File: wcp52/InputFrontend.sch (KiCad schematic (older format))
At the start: 8 parts

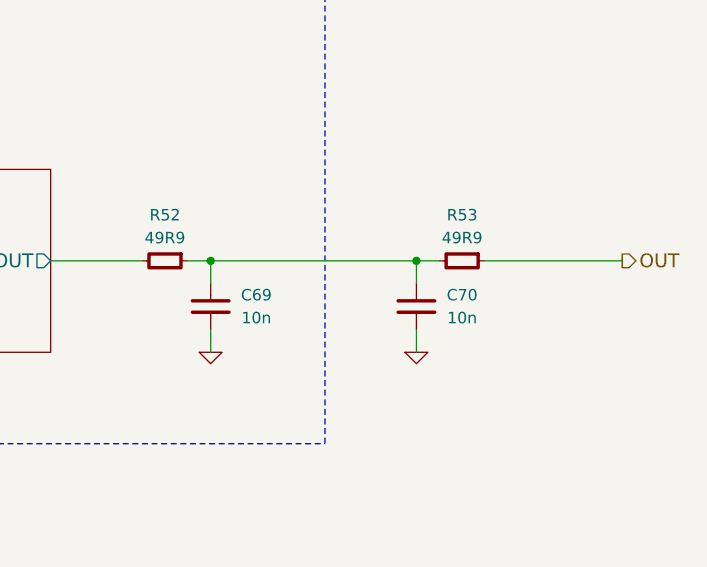
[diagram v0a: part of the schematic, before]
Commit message: Add PSU filter inductors
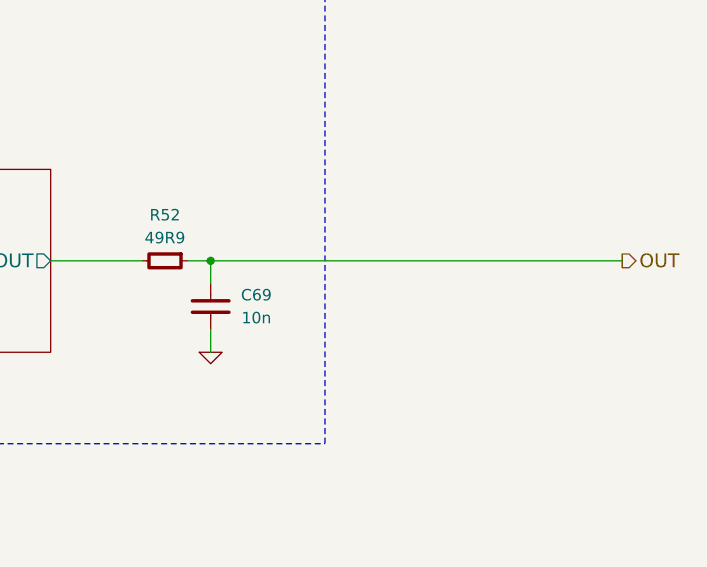
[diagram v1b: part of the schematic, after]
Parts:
- removed C70: 10n, IPC7351-Nominal:CAPC1608X55, symbol C-0603
- removed R53: 49R9, IPC7351-Nominal:RESC1608X50, symbol R-0603
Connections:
- net OUT: now also C69.1, R52.1
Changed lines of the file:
@@
 $EndComp
 $Comp
-L GND #PWR0150
+L GND #PWR0151
 U 1 1 54F2F4A0
 P 3500 4300
-F 0 "#PWR0150" H 3500 4300 30  0001 C CNN
+F 0 "#PWR0151" H 3500 4300 30  0001 C CNN
 F 1 "GND" H 3500 4230 30  0001 C CNN
 F 2 "" H 3500 4300 60  0000 C CNN
@@
 	10300 1200 3200 1200
 Wire Wire Line
-	9700 3400 10800 3400
+	9700 3400 11600 3400
 Wire Wire Line
 	9800 3400 9800 3500
 Connection ~ 9800 3400
-Wire Wire Line
-	10700 3400 10700 3500
-Connection ~ 10700 3400
 Text HLabel 11600 3400 2    60   Output ~ 0
 OUT
-Wire Wire Line
-	11600 3400 11000 3400
-$Comp
-L GND #PWR0151
+$Comp
+L GND #PWR0152
 U 1 1 54F3075A
 P 9800 3800
-F 0 "#PWR0151" H 9800 3800 30  0001 C CNN
+F 0 "#PWR0152" H 9800 3800 30  0001 C CNN
 F 1 "GND" H 9800 3730 30  0001 C CNN
 F 2 "" H 9800 3800 60  0000 C CNN
@@
 Wire Wire Line
 	9800 3700 9800 3800
-$Comp
-L GND #PWR0152
-U 1 1 54F3079D
-P 10700 3800
-F 0 "#PWR0152" H 10700 3800 30  0001 C CNN
-F 1 "GND" H 10700 3730 30  0001 C CNN
-F 2 "" H 10700 3800 60  0000 C CNN
-F 3 "" H 10700 3800 60  0000 C CNN
-	1    10700 3800
-	1    0    0    -1
-$EndComp
-Wire Wire Line
-	10700 3800 10700 3700
 Wire Wire Line
 	4300 3200 1800 3200
@@
 F 5 "CAP MLCC 10n ≥X5R 50V 10% [0603]" H 10600 4150 60  0001 C CNN "BOM"
 	1    9800 3600
-	1    0    0    -1
-$EndComp
-$Comp
-L C-0603 C70
-U 1 1 55033D91
-P 10700 3600
-F 0 "C70" H 10900 3650 50  0000 C CNN
-F 1 "10n" H 10900 3550 50  0000 C CNN
-F 2 "IPC7351-Nominal:CAPC1608X55" H 10700 3600 50  0001 C CNN
-F 3 "" H 10690 3575 60  0000 C CNN
-F 4 "Value" H 10700 3600 60  0001 C CNN "Manuf"
-F 5 "CAP MLCC 10n ≥X5R 50V 10% [0603]" H 11500 4150 60  0001 C CNN "BOM"
-	1    10700 3600
 	1    0    0    -1
 $EndComp
@@
 	0    1    1    0
 $EndComp
-$Comp
-L R-0603 R53
-U 1 1 550340A6
-P 10900 3400
-F 0 "R53" V 10700 3400 50  0000 C CNN
-F 1 "49R9" V 10800 3400 50  0000 C CNN
-F 2 "IPC7351-Nominal:RESC1608X50" H 10900 3400 50  0001 C CNN
-F 3 "" H 10900 3450 60  0000 C CNN
-F 4 "Value" H 10900 3400 60  0001 C CNN "Manuf"
-F 5 "RES SMD 49R9 1% [0603]" H 11650 3950 60  0001 C CNN "BOM"
-	1    10900 3400
-	0    1    1    0
-$EndComp

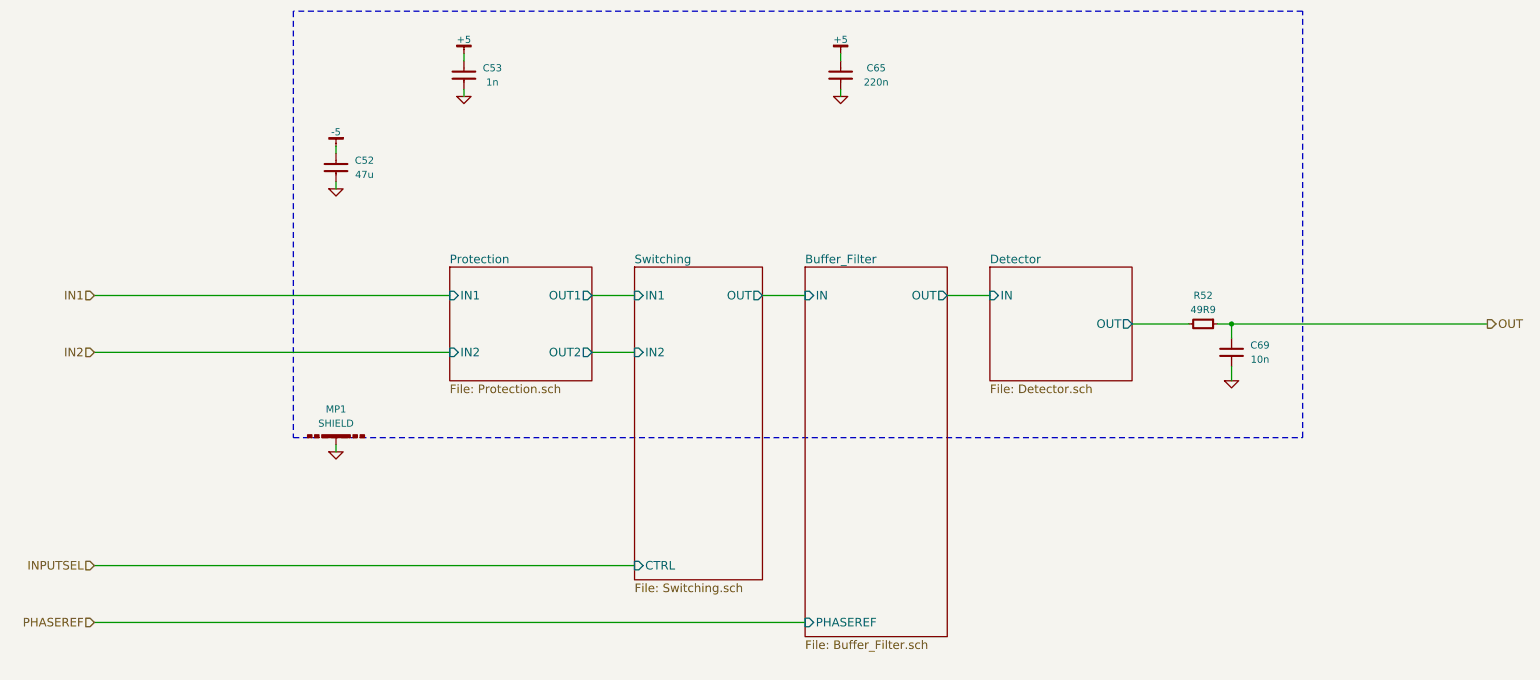
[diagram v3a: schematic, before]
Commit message: Reannotate parts. May need to tweak silkscreen
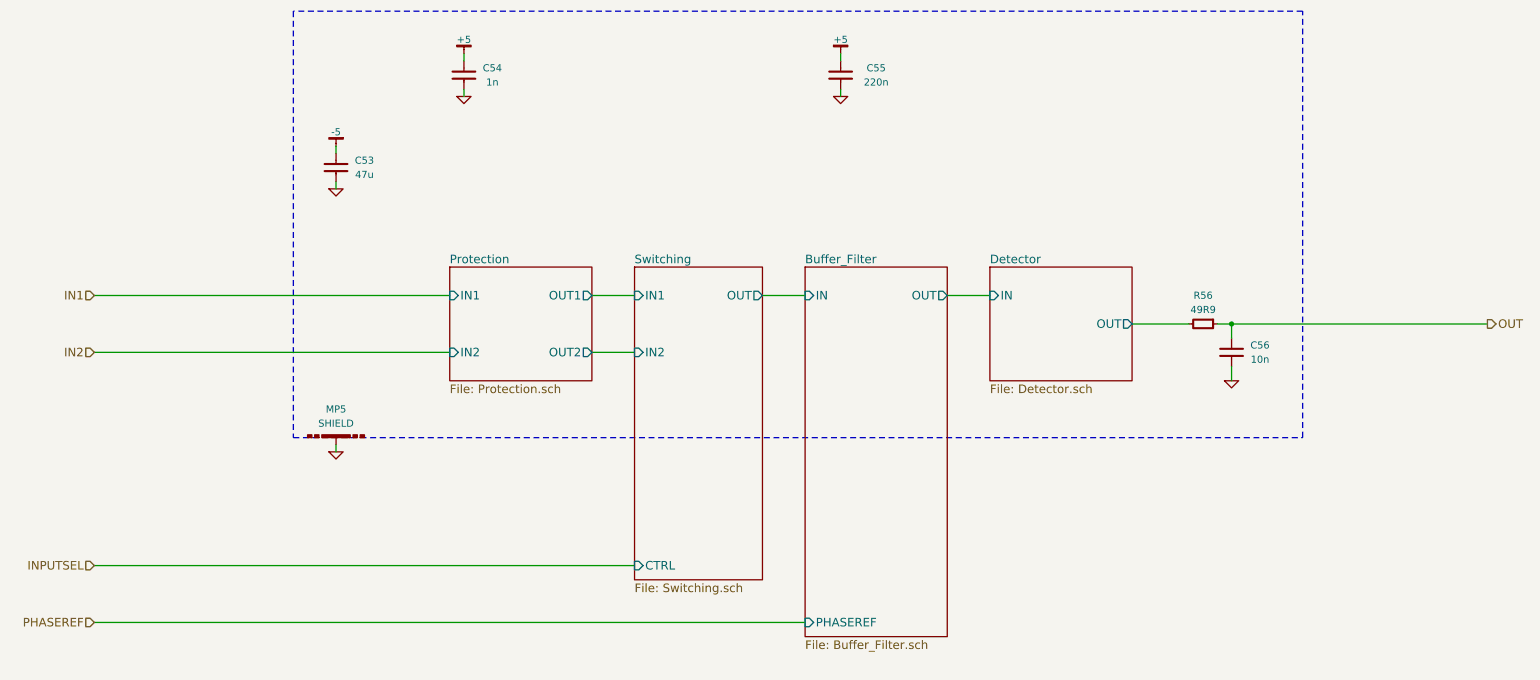
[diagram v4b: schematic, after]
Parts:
- C53: renamed from C52; OldReference (none) -> C52
- C54: renamed from C53; OldReference (none) -> C53
- C55: renamed from C65; OldReference (none) -> C65
- C56: renamed from C69; OldReference (none) -> C69
- MP5: renamed from MP1; OldReference (none) -> MP1
- R56: renamed from R52; OldReference (none) -> R52
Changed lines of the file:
@@
 $EndDescr
 $Comp
-L SHIELD MP1
+L SHIELD MP5
 U 1 1 54F2F3A6
 P 3500 4200
-F 0 "MP1" H 3500 4400 50  0000 C CNN
+F 0 "MP5" H 3500 4400 50  0000 C CNN
 F 1 "SHIELD" H 3500 4300 50  0000 C CNN
 F 2 "manuf:LAIRD-BMI-S-203" H 3500 4200 50  0001 C CNN
@@
 F 5 "Laird" H 3500 4200 60  0001 C CNN "Manuf"
 F 6 "DIST DIGIKEY 903-1052-1-ND; DIST DIGIKEY 903-1015-ND" H 3500 4200 60  0001 C CNN "BOM"
+F 7 "MP1" H 3500 4200 50  0001 C CNN "OldReference"
 	1    3500 4200
 	1    0    0    -1
@@
 F 2 "" H 3500 4300 60  0000 C CNN
 F 3 "" H 3500 4300 60  0000 C CNN
+F 4 "#PWR0163" H 3500 4300 50  0001 C CNN "OldReference"
 	1    3500 4300
 	1    0    0    -1
@@
 F 2 "" H 9800 3800 60  0000 C CNN
 F 3 "" H 9800 3800 60  0000 C CNN
+F 4 "#PWR0164" H 9800 3800 50  0001 C CNN "OldReference"
 	1    9800 3800
 	1    0    0    -1
@@
 	9100 3400 9500 3400
 $Comp
-L C-1206 C52
+L C-1206 C53
 U 1 1 54F26D26
 P 3500 2300
-F 0 "C52" H 3700 2350 50  0000 C CNN
+F 0 "C53" H 3700 2350 50  0000 C CNN
 F 1 "47u" H 3700 2250 50  0000 C CNN
 F 2 "IPC7351-Nominal:CAPC3216X70" H 3500 2300 50  0001 C CNN
@@
 F 4 "Value" H 3500 2300 60  0001 C CNN "Manuf"
 F 5 "CAP MLCC 47u ≥X5R 10V 20% [1206]" H 4300 2850 60  0001 C CNN "BOM"
+F 6 "C52" H 3500 2300 50  0001 C CNN "OldReference"
 	1    3500 2300
 	1    0    0    -1
@@
 F 2 "" H 3500 2150 60  0000 C CNN
 F 3 "" H 3500 2150 60  0000 C CNN
+F 4 "#PWR0165" H 3500 2150 50  0001 C CNN "OldReference"
 	1    3500 2150
 	-1   0    0    1
@@
 F 2 "" H 3500 2450 60  0000 C CNN
 F 3 "" H 3500 2450 60  0000 C CNN
+F 4 "#PWR0166" H 3500 2450 50  0001 C CNN "OldReference"
 	1    3500 2450
 	1    0    0    -1
@@
 F 2 "" H 4400 1800 60  0000 C CNN
 F 3 "" H 4400 1800 60  0000 C CNN
+F 4 "#PWR0167" H 4400 1800 50  0001 C CNN "OldReference"
 	1    4400 1800
 	1    0    0    -1
@@
 F 2 "" H 4400 1500 60  0000 C CNN
 F 3 "" H 4400 1500 60  0000 C CNN
+F 4 "#PWR0168" H 4400 1500 50  0001 C CNN "OldReference"
 	1    4400 1500
 	1    0    0    -1
 $EndComp
 $Comp
-L C-0805 C65
+L C-0805 C55
 U 1 1 54F29C49
 P 7050 1650
-F 0 "C65" H 7300 1700 50  0000 C CNN
+F 0 "C55" H 7300 1700 50  0000 C CNN
 F 1 "220n" H 7300 1600 50  0000 C CNN
 F 2 "IPC7351-Nominal:CAPC2012X70" H 7050 1650 50  0001 C CNN
@@
 F 4 "Value" H 7050 1650 60  0001 C CNN "Manuf"
 F 5 "CAP MLCC 220n ≥X5R 16V 10% [0805]" H 7850 2200 60  0001 C CNN "BOM"
+F 6 "C65" H 7050 1650 50  0001 C CNN "OldReference"
 	1    7050 1650
 	1    0    0    -1
@@
 F 2 "" H 7050 1800 60  0000 C CNN
 F 3 "" H 7050 1800 60  0000 C CNN
+F 4 "#PWR0169" H 7050 1800 50  0001 C CNN "OldReference"
 	1    7050 1800
 	1    0    0    -1
@@
 F 2 "" H 7050 1500 60  0000 C CNN
 F 3 "" H 7050 1500 60  0000 C CNN
+F 4 "#PWR0170" H 7050 1500 50  0001 C CNN "OldReference"
 	1    7050 1500
 	1    0    0    -1
 $EndComp
 $Comp
-L C-0603 C53
+L C-0603 C54
 U 1 1 5502DDEE
 P 4400 1650
-F 0 "C53" H 4600 1700 50  0000 C CNN
+F 0 "C54" H 4600 1700 50  0000 C CNN
 F 1 "1n" H 4600 1600 50  0000 C CNN
 F 2 "IPC7351-Nominal:CAPC1608X55" H 4400 1650 50  0001 C CNN
@@
 F 4 "Value" H 4400 1650 60  0001 C CNN "Manuf"
 F 5 "CAP MLCC 1n C0G 50V 10% [0603]" H 5200 2200 60  0001 C CNN "BOM"
+F 6 "C53" H 4400 1650 50  0001 C CNN "OldReference"
 	1    4400 1650
 	1    0    0    -1
 $EndComp
 $Comp
-L C-0603 C69
+L C-0603 C56
 U 1 1 55033561
 P 9800 3600
-F 0 "C69" H 10000 3650 50  0000 C CNN
+F 0 "C56" H 10000 3650 50  0000 C CNN
 F 1 "10n" H 10000 3550 50  0000 C CNN
 F 2 "IPC7351-Nominal:CAPC1608X55" H 9800 3600 50  0001 C CNN
@@
 F 4 "Value" H 9800 3600 60  0001 C CNN "Manuf"
 F 5 "CAP MLCC 10n ≥X5R 50V 10% [0603]" H 10600 4150 60  0001 C CNN "BOM"
+F 6 "C69" H 9800 3600 50  0001 C CNN "OldReference"
 	1    9800 3600
 	1    0    0    -1
 $EndComp
 $Comp
-L R-0603 R52
+L R-0603 R56
 U 1 1 55033DF8
 P 9600 3400
-F 0 "R52" V 9400 3400 50  0000 C CNN
+F 0 "R56" V 9400 3400 50  0000 C CNN
 F 1 "49R9" V 9500 3400 50  0000 C CNN
 F 2 "IPC7351-Nominal:RESC1608X50" H 9600 3400 50  0001 C CNN
@@
 F 4 "Value" H 9600 3400 60  0001 C CNN "Manuf"
 F 5 "RES SMD 49R9 1% [0603]" H 10350 3950 60  0001 C CNN "BOM"
+F 6 "R52" H 9600 3400 50  0001 C CNN "OldReference"
 	1    9600 3400
 	0    1    1    0

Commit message: Schematic touchups
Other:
- moved on the sheet: C53, C54, C55
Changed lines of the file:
@@
 Sheet 6 13
 Title "Input Frontend"
-Date "2015-03-10"
+Date "2015-03-13"
 Rev ""
 Comp "WCP52"
@@
 L C-1206 C53
 U 1 1 54F26D26
-P 3500 2300
-F 0 "C53" H 3700 2350 50  0000 C CNN
-F 1 "47u" H 3700 2250 50  0000 C CNN
-F 2 "IPC7351-Nominal:CAPC3216X70" H 3500 2300 50  0001 C CNN
-F 3 "" H 3490 2275 60  0000 C CNN
-F 4 "Value" H 3500 2300 60  0001 C CNN "Manuf"
-F 5 "CAP MLCC 47u ≥X5R 10V 20% [1206]" H 4300 2850 60  0001 C CNN "BOM"
-F 6 "C52" H 3500 2300 50  0001 C CNN "OldReference"
-	1    3500 2300
+P 3500 1650
+F 0 "C53" H 3700 1700 50  0000 C CNN
+F 1 "47u" H 3700 1600 50  0000 C CNN
+F 2 "IPC7351-Nominal:CAPC3216X70" H 3500 1650 50  0001 C CNN
+F 3 "" H 3490 1625 60  0000 C CNN
+F 4 "Value" H 3500 1650 60  0001 C CNN "Manuf"
+F 5 "CAP MLCC 47u ≥X5R 10V 20% [1206]" H 4300 2200 60  0001 C CNN "BOM"
+F 6 "C52" H 3500 1650 50  0001 C CNN "OldReference"
+	1    3500 1650
 	1    0    0    -1
 $EndComp
@@
 L -5 #PWR0165
 U 1 1 54F26D5C
-P 3500 2150
-F 0 "#PWR0165" H 3500 2100 30  0001 C CNN
-F 1 "-5" H 3500 2050 50  0000 C CNN
-F 2 "" H 3500 2150 60  0000 C CNN
-F 3 "" H 3500 2150 60  0000 C CNN
-F 4 "#PWR0165" H 3500 2150 50  0001 C CNN "OldReference"
-	1    3500 2150
+P 3500 1500
+F 0 "#PWR0165" H 3500 1450 30  0001 C CNN
+F 1 "-5" H 3500 1400 50  0000 C CNN
+F 2 "" H 3500 1500 60  0000 C CNN
+F 3 "" H 3500 1500 60  0000 C CNN
+F 4 "#PWR0165" H 3500 1500 50  0001 C CNN "OldReference"
+	1    3500 1500
 	-1   0    0    1
 $EndComp
 Wire Wire Line
-	3500 2150 3500 2200
+	3500 1500 3500 1550
 $Comp
 L GND #PWR0166
 U 1 1 54F26E11
-P 3500 2450
-F 0 "#PWR0166" H 3500 2450 30  0001 C CNN
-F 1 "GND" H 3500 2380 30  0001 C CNN
-F 2 "" H 3500 2450 60  0000 C CNN
-F 3 "" H 3500 2450 60  0000 C CNN
-F 4 "#PWR0166" H 3500 2450 50  0001 C CNN "OldReference"
-	1    3500 2450
-	1    0    0    -1
-$EndComp
-Wire Wire Line
-	3500 2450 3500 2400
-Wire Wire Line
-	4400 1500 4400 1550
+P 3500 1800
+F 0 "#PWR0166" H 3500 1800 30  0001 C CNN
+F 1 "GND" H 3500 1730 30  0001 C CNN
+F 2 "" H 3500 1800 60  0000 C CNN
+F 3 "" H 3500 1800 60  0000 C CNN
+F 4 "#PWR0166" H 3500 1800 50  0001 C CNN "OldReference"
+	1    3500 1800
+	1    0    0    -1
+$EndComp
+Wire Wire Line
+	3500 1800 3500 1750
+Wire Wire Line
+	3950 1500 3950 1550
 $Comp
 L GND #PWR0167
 U 1 1 54F288BE
+P 3950 1800
+F 0 "#PWR0167" H 3950 1800 30  0001 C CNN
+F 1 "GND" H 3950 1730 30  0001 C CNN
+F 2 "" H 3950 1800 60  0000 C CNN
+F 3 "" H 3950 1800 60  0000 C CNN
+F 4 "#PWR0167" H 3950 1800 50  0001 C CNN "OldReference"
+	1    3950 1800
+	1    0    0    -1
+$EndComp
+Wire Wire Line
+	3950 1800 3950 1750
+$Comp
+L +5 #PWR0168
+U 1 1 54F2892E
+P 3950 1500
+F 0 "#PWR0168" H 3950 1550 30  0001 C CNN
+F 1 "+5" H 3950 1600 50  0000 C CNN
+F 2 "" H 3950 1500 60  0000 C CNN
+F 3 "" H 3950 1500 60  0000 C CNN
+F 4 "#PWR0168" H 3950 1500 50  0001 C CNN "OldReference"
+	1    3950 1500
+	1    0    0    -1
+$EndComp
+$Comp
+L C-0805 C55
+U 1 1 54F29C49
+P 4400 1650
+F 0 "C55" H 4650 1700 50  0000 C CNN
+F 1 "220n" H 4650 1600 50  0000 C CNN
+F 2 "IPC7351-Nominal:CAPC2012X70" H 4400 1650 50  0001 C CNN
+F 3 "" H 4390 1625 60  0000 C CNN
+F 4 "Value" H 4400 1650 60  0001 C CNN "Manuf"
+F 5 "CAP MLCC 220n ≥X5R 16V 10% [0805]" H 5200 2200 60  0001 C CNN "BOM"
+F 6 "C65" H 4400 1650 50  0001 C CNN "OldReference"
+	1    4400 1650
+	1    0    0    -1
+$EndComp
+Wire Wire Line
+	4400 1500 4400 1550
+$Comp
+L GND #PWR0169
+U 1 1 54F29C50
 P 4400 1800
-F 0 "#PWR0167" H 4400 1800 30  0001 C CNN
+F 0 "#PWR0169" H 4400 1800 30  0001 C CNN
 F 1 "GND" H 4400 1730 30  0001 C CNN
 F 2 "" H 4400 1800 60  0000 C CNN
 F 3 "" H 4400 1800 60  0000 C CNN
-F 4 "#PWR0167" H 4400 1800 50  0001 C CNN "OldReference"
+F 4 "#PWR0169" H 4400 1800 50  0001 C CNN "OldReference"
 	1    4400 1800
 	1    0    0    -1
@@
 	4400 1800 4400 1750
 $Comp
-L +5 #PWR0168
-U 1 1 54F2892E
+L +5 #PWR0170
+U 1 1 54F29C57
 P 4400 1500
-F 0 "#PWR0168" H 4400 1550 30  0001 C CNN
+F 0 "#PWR0170" H 4400 1550 30  0001 C CNN
 F 1 "+5" H 4400 1600 50  0000 C CNN
 F 2 "" H 4400 1500 60  0000 C CNN
 F 3 "" H 4400 1500 60  0000 C CNN
-F 4 "#PWR0168" H 4400 1500 50  0001 C CNN "OldReference"
+F 4 "#PWR0170" H 4400 1500 50  0001 C CNN "OldReference"
 	1    4400 1500
-	1    0    0    -1
-$EndComp
-$Comp
-L C-0805 C55
-U 1 1 54F29C49
-P 7050 1650
-F 0 "C55" H 7300 1700 50  0000 C CNN
-F 1 "220n" H 7300 1600 50  0000 C CNN
-F 2 "IPC7351-Nominal:CAPC2012X70" H 7050 1650 50  0001 C CNN
-F 3 "" H 7040 1625 60  0000 C CNN
-F 4 "Value" H 7050 1650 60  0001 C CNN "Manuf"
-F 5 "CAP MLCC 220n ≥X5R 16V 10% [0805]" H 7850 2200 60  0001 C CNN "BOM"
-F 6 "C65" H 7050 1650 50  0001 C CNN "OldReference"
-	1    7050 1650
-	1    0    0    -1
-$EndComp
-Wire Wire Line
-	7050 1500 7050 1550
-$Comp
-L GND #PWR0169
-U 1 1 54F29C50
-P 7050 1800
-F 0 "#PWR0169" H 7050 1800 30  0001 C CNN
-F 1 "GND" H 7050 1730 30  0001 C CNN
-F 2 "" H 7050 1800 60  0000 C CNN
-F 3 "" H 7050 1800 60  0000 C CNN
-F 4 "#PWR0169" H 7050 1800 50  0001 C CNN "OldReference"
-	1    7050 1800
-	1    0    0    -1
-$EndComp
-Wire Wire Line
-	7050 1800 7050 1750
-$Comp
-L +5 #PWR0170
-U 1 1 54F29C57
-P 7050 1500
-F 0 "#PWR0170" H 7050 1550 30  0001 C CNN
-F 1 "+5" H 7050 1600 50  0000 C CNN
-F 2 "" H 7050 1500 60  0000 C CNN
-F 3 "" H 7050 1500 60  0000 C CNN
-F 4 "#PWR0170" H 7050 1500 50  0001 C CNN "OldReference"
-	1    7050 1500
 	1    0    0    -1
 $EndComp
@@
 L C-0603 C54
 U 1 1 5502DDEE
-P 4400 1650
-F 0 "C54" H 4600 1700 50  0000 C CNN
-F 1 "1n" H 4600 1600 50  0000 C CNN
-F 2 "IPC7351-Nominal:CAPC1608X55" H 4400 1650 50  0001 C CNN
-F 3 "" H 4390 1625 60  0000 C CNN
-F 4 "Value" H 4400 1650 60  0001 C CNN "Manuf"
-F 5 "CAP MLCC 1n C0G 50V 10% [0603]" H 5200 2200 60  0001 C CNN "BOM"
-F 6 "C53" H 4400 1650 50  0001 C CNN "OldReference"
-	1    4400 1650
-	1    0    0    -1
-$EndComp
+P 3950 1650
+F 0 "C54" H 4150 1700 50  0000 C CNN
+F 1 "1n" H 4150 1600 50  0000 C CNN
+F 2 "IPC7351-Nominal:CAPC1608X55" H 3950 1650 50  0001 C CNN
+F 3 "" H 3940 1625 60  0000 C CNN
+F 4 "Value" H 3950 1650 60  0001 C CNN "Manuf"
+F 5 "CAP MLCC 1n C0G 50V 10% [0603]" H 4750 2200 60  0001 C CNN "BOM"
+F 6 "C53" H 3950 1650 50  0001 C CNN "OldReference"
+	1    3950 1650
+	1    0    0    -1
+$EndComp
